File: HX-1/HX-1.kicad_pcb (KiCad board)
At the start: 2 copper layers, 45 x 90 mm, 92 parts, among them J1 USB_C_Receptacle_USB2.0_16P, J10 Conn_01x24, J11 Conn_01x08, J12 USART, J2 Conn_01x02_Socket, J3 I2C, J4 SPI, J6 DEBUG, J8 UART, J9 Conn_01x24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

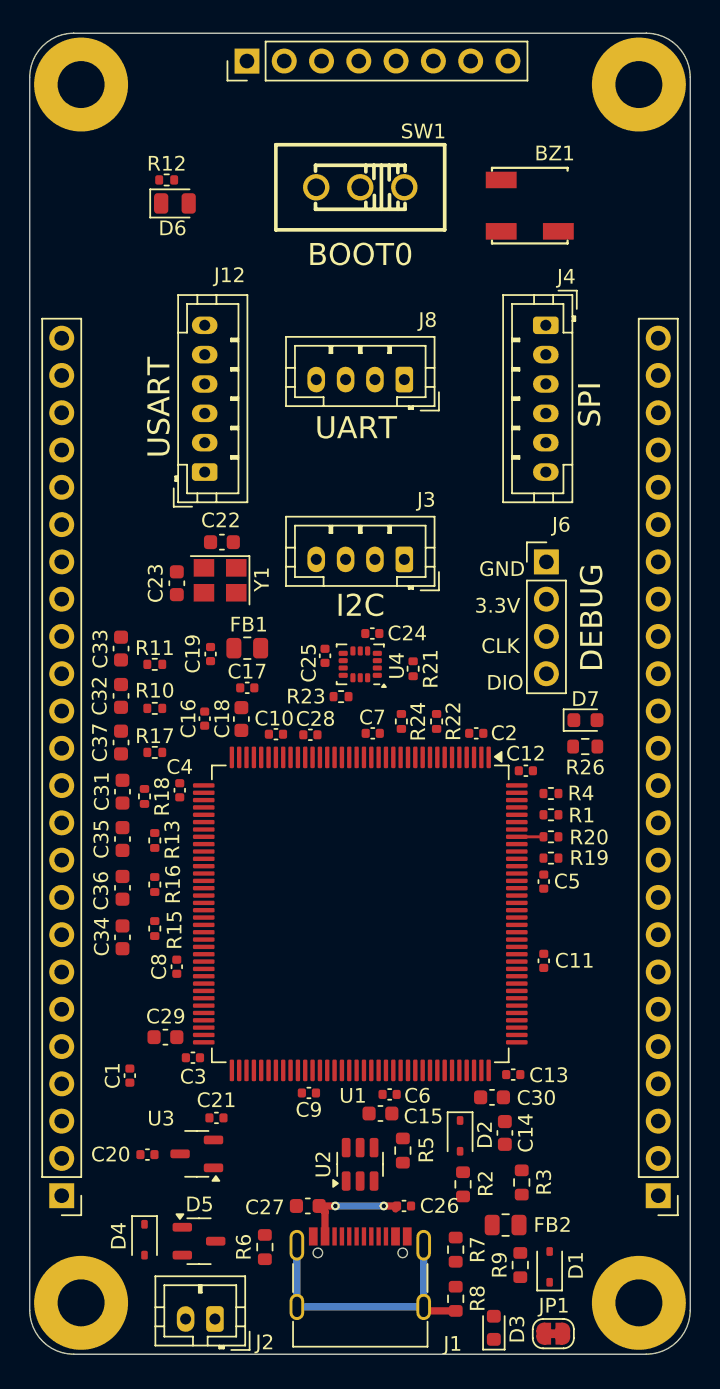
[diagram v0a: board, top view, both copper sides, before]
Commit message: complete initial placement of all components, trace 5V
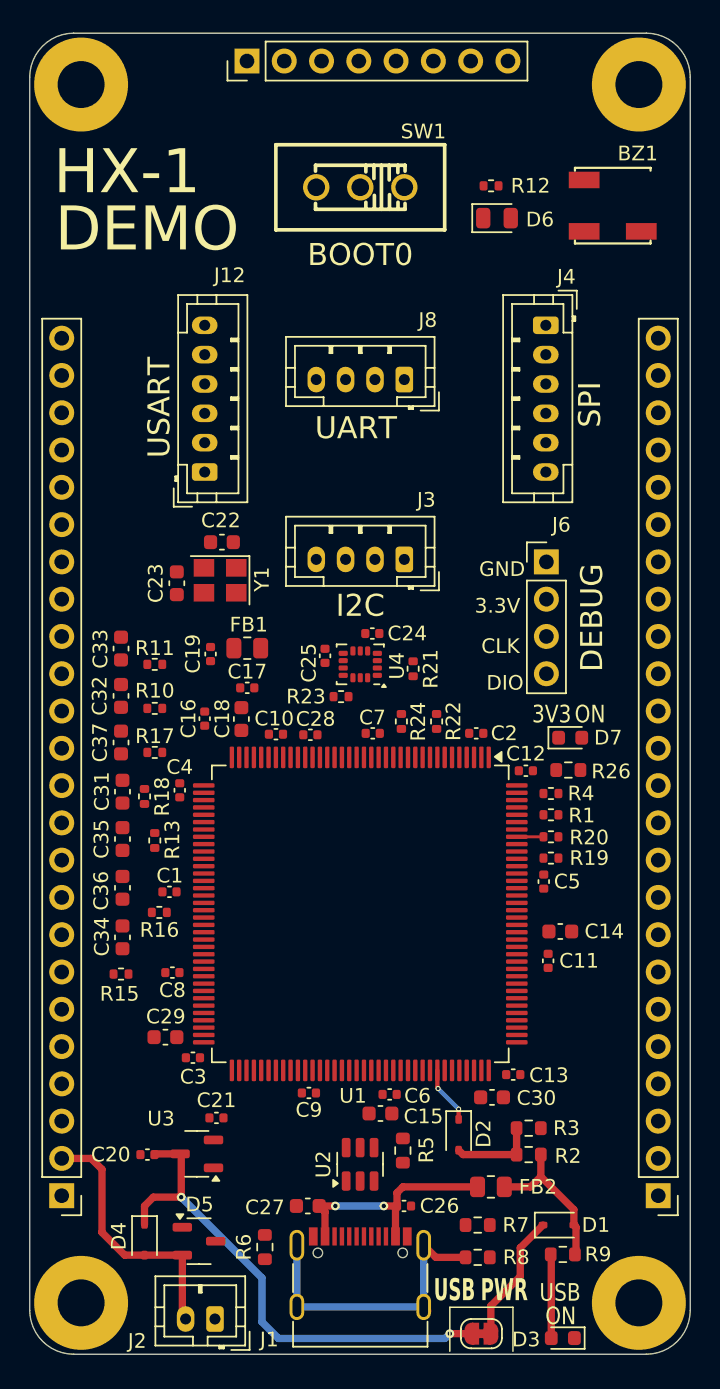
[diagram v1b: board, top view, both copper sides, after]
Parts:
- moved R12 22.1 mm to (153.9, 67.4)
- moved D6 22.0 mm to (154.3, 69.6)
- moved C14 14.2 mm to (158.6, 118.2), turned to 0 degrees
- moved C1 12.8 mm to (132.0, 115.5), turned to 180 degrees
- moved BZ1 5.65 mm to (162.0, 62.8)
- moved R2 4.91 mm to (156.5, 133.4), turned to 180 degrees
- moved JP1 4.90 mm to (153.2, 145.6), turned to 180 degrees
- moved D3 4.75 mm to (158.8, 145.9), turned to 180 degrees
- moved R15 3.86 mm to (128.7, 121.1), turned to 180 degrees
- moved R3 3.73 mm to (156.5, 131.6), turned to 0 degrees
- moved R8 3.20 mm to (153.0, 140.4), turned to 0 degrees
- moved R9 2.99 mm to (158.8, 140.2), turned to 0 degrees
- moved D1 2.91 mm to (158.5, 138.2), turned to 0 degrees
- moved FB2 2.79 mm to (153.9, 135.6)
- moved R7 2.25 mm to (153.0, 138.2), turned to 180 degrees
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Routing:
- net +5V: track 0.00 -> 34.4 mm, vias 0 -> 2
- net V_BATT_RAW: track 0.00 -> 17.9 mm
- net VBUS: track 0.00 -> 10.6 mm
- net /Communication and Debug/VBUS_bridge: track 0.00 -> 8.87 mm
- net vbus_source: track 7.68 -> 16.4 mm
- net /Communication and Debug/vbus_r_divider: track 0.00 -> 5.87 mm
- net /Communication and Debug/USB_LED: track 0.00 -> 5.72 mm
- net USB_VBUS_SENSE: track 0.00 -> 3.94 mm, vias 0 -> 2
- net /Communication and Debug/USB_Shield: track 19.3 -> 20.6 mm
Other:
- board text added: "3V3"
- board text added: "DEMO"
- board text added: "HX-1"
- board text added: "ON"
- board text added: "PWR"
- board text added: "USB"

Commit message: remove 8 pin header on top of board, extend side headers by 4 each to replace pins
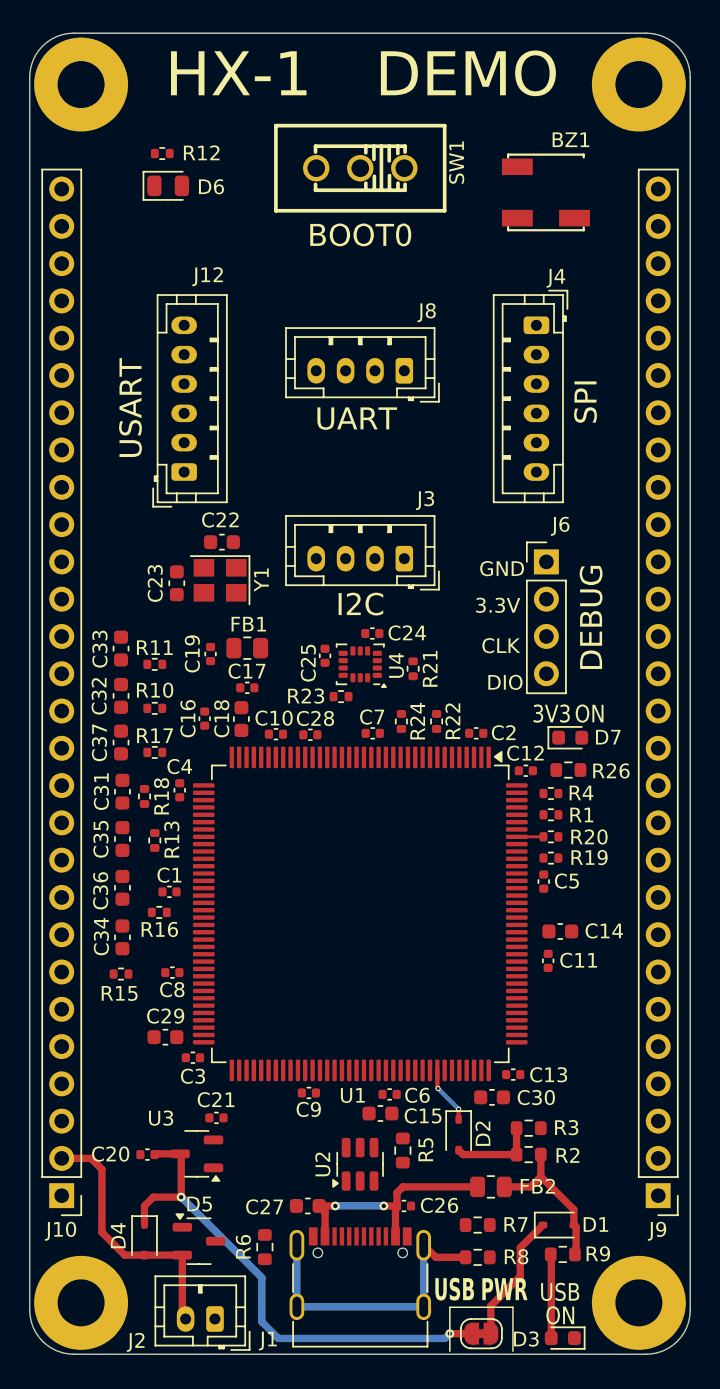
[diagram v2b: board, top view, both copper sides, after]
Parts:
- removed J11: Conn_01x08, Connector_PinHeader_2.54mm:PinHeader_1x08_P2.54mm_Vertical
- J10, J9: footprint Connector_PinHeader_2.54mm:PinHeader_1x24_P2.54mm_Vertical -> Connector_PinHeader_2.54mm:PinHeader_1x28_P2.54mm_Vertical
- moved R12 22.5 mm to (131.5, 65.2)
- moved D6 22.5 mm to (131.9, 67.4)
- moved BZ1 4.64 mm to (157.4, 61.9)
- moved J12 1.40 mm to (133.0, 86.9)
- moved SW1 1.30 mm to (145.0, 66.2)
- moved J4 0.64 mm to (157.0, 76.9)
- moved J8 0.60 mm to (148.0, 80.0)

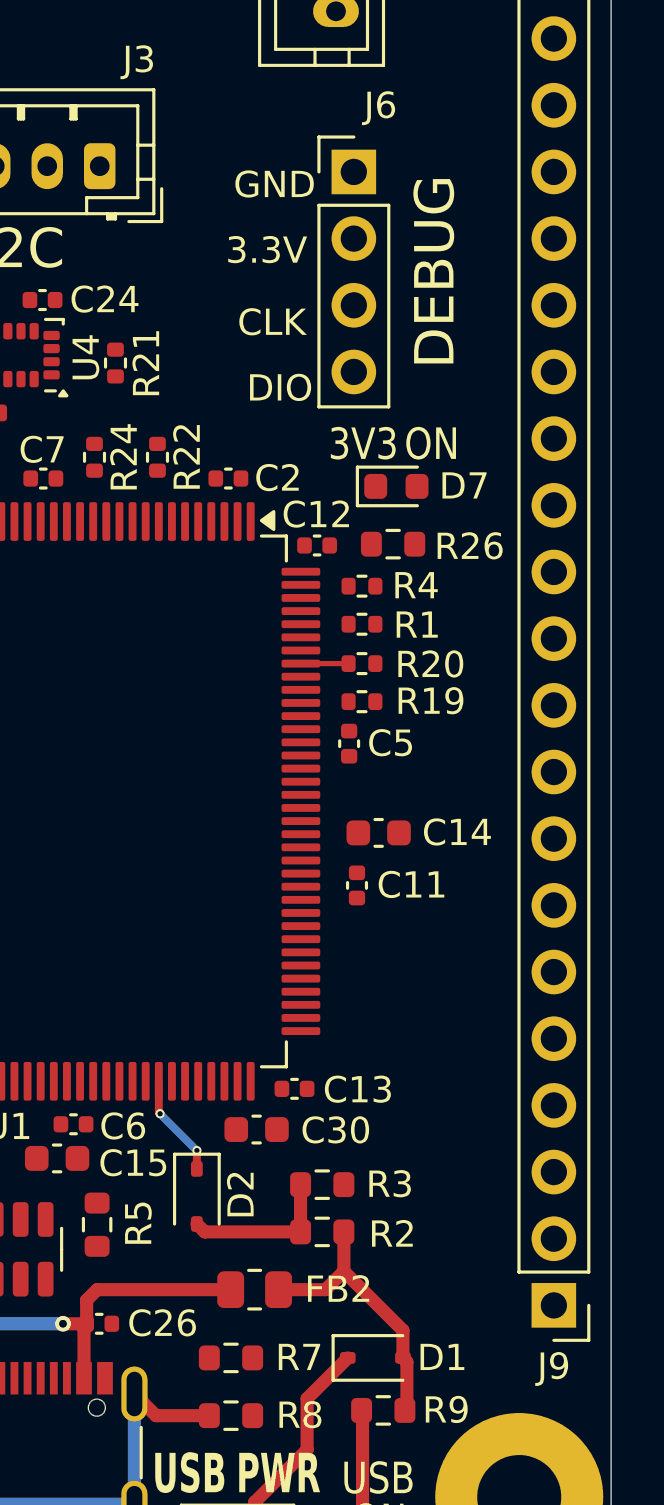
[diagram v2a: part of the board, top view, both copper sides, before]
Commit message: remove GPIO 12 and DEBUG conn, add debug to right header
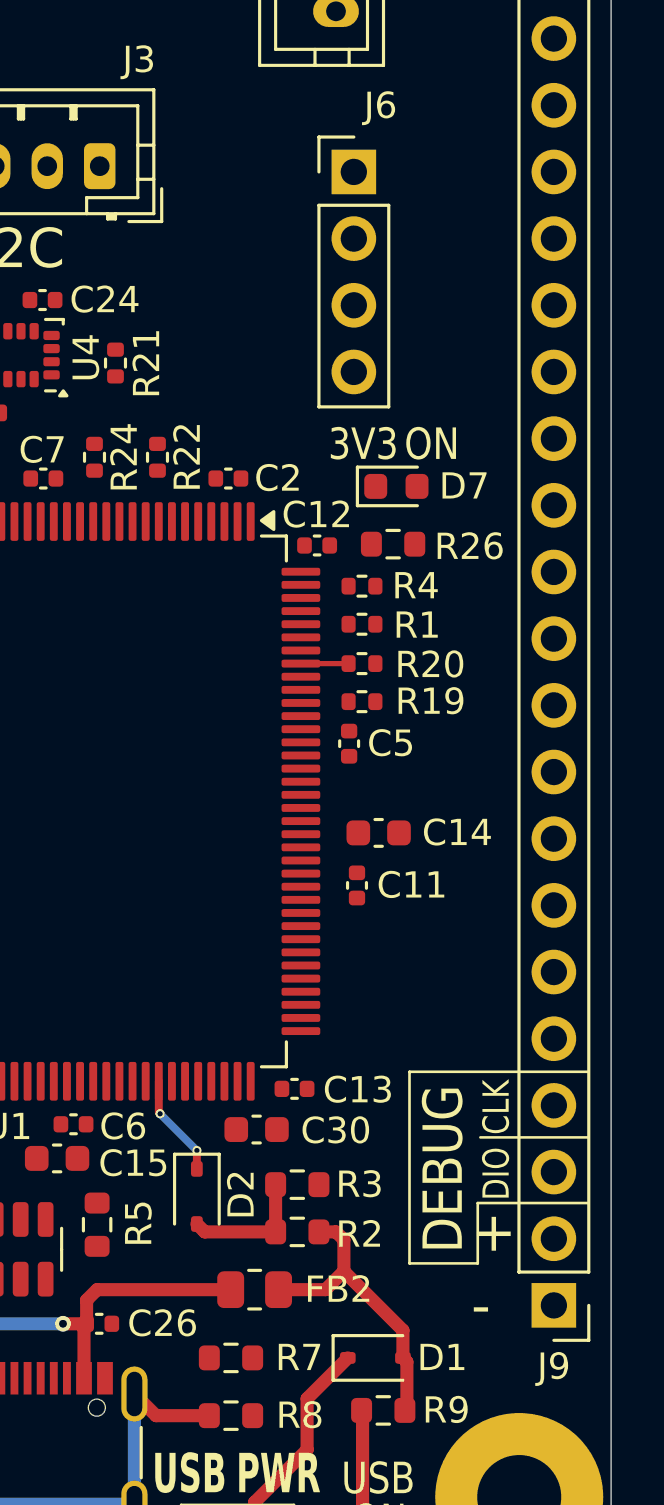
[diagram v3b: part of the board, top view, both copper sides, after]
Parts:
- moved R2 0.95 mm to (155.5, 133.4)
- moved R3 0.95 mm to (155.5, 131.6)
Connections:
- J10 pad 20: /MCU/TIM1_PWM_1- -> /MCU/TIM4_PWM_3
- J10 pad 21: /MCU/TIM1_PWM_1+ -> /MCU/TIM4_PWM_4
- J10 pad 22: /MCU/GPIO_12 -> /MCU/TIM1_PWM_1-
- J10 pad 23: /MCU/GPIO_11 -> /MCU/TIM1_PWM_1+
- J10 pad 24: /MCU/GPIO_10 -> /MCU/GPIO_11
- J10 pad 25: /MCU/GPIO_9 -> /MCU/GPIO_10
- J10 pad 26: /MCU/GPIO_8 -> /MCU/GPIO_9
- J10 pad 27: unconnected-(J10-Pin_27-Pad27) -> /MCU/GPIO_8
- J9 pad 3: /MCU/TIM4_PWM_4 -> /MCU/DEBUG_SWDIO
- J9 pad 4: /MCU/TIM4_PWM_3 -> /MCU/DEBUG_SWCLK
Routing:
- net /Communication and Debug/vbus_r_divider: track 5.87 -> 4.92 mm
- net VBUS: track 10.6 -> 11.3 mm
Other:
- board text added: "+"
- board text added: "-"
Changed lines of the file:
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@@
 	(net 152 "/MCU/DEBUG_SWDIO")
 	(net 153 "/MCU/DEBUG_SWCLK")
-	(net 154 "unconnected-(J10-Pin_27-Pad27)")
 	(footprint "Capacitor_SMD:C_0402_1005Metric"
 		(layer "F.Cu")
@@
 			)
 			(remove_unused_layers no)
-			(net 61 "/MCU/TIM4_PWM_4")
+			(net 152 "/MCU/DEBUG_SWDIO")
 			(pinfunction "Pin_3")
 			(pintype "passive")
@@
 			)
 			(remove_unused_layers no)
-			(net 56 "/MCU/TIM4_PWM_3")
+			(net 153 "/MCU/DEBUG_SWCLK")
 			(pinfunction "Pin_4")
 			(pintype "passive")
@@
 	(footprint "Resistor_SMD:R_0603_1608Metric"
 		(layer "F.Cu")
-		(at 156.475 133.4 180)
+		(at 155.525 133.4 180)
 		(descr "Resistor SMD 0603 (1608 Metric), square (rectangular) end terminal, IPC_7351 nominal, (Body size source: IPC-SM-782 page 72, https://www.pcb-3d.com/wordpress/wp-content/uploads/ipc-sm-782a_amendment_1_and_2.pdf), generated with kicad-footprint-generator")
 		(tags "resistor")
 		(property "Reference" "R2"
-			(at -2.675 -0.1 0)
+			(at -2.375 -0.1 0)
 			(layer "F.SilkS")
 			(effects
@@
 			)
 			(remove_unused_layers no)
-			(net 82 "/MCU/TIM1_PWM_1-")
+			(net 56 "/MCU/TIM4_PWM_3")
 			(pinfunction "Pin_20")
 			(pintype "passive")
@@
 			)
 			(remove_unused_layers no)
-			(net 92 "/MCU/TIM1_PWM_1+")
+			(net 61 "/MCU/TIM4_PWM_4")
 			(pinfunction "Pin_21")
 			(pintype "passive")
@@
 			)
 			(remove_unused_layers no)
-			(net 144 "/MCU/GPIO_12")
+			(net 82 "/MCU/TIM1_PWM_1-")
 			(pinfunction "Pin_22")
 			(pintype "passive")
@@
 			)
 			(remove_unused_layers no)
-			(net 142 "/MCU/GPIO_11")
+			(net 92 "/MCU/TIM1_PWM_1+")
 			(pinfunction "Pin_23")
 			(pintype "passive")
@@
 			)
 			(remove_unused_layers no)
-			(net 146 "/MCU/GPIO_10")
+			(net 142 "/MCU/GPIO_11")
 			(pinfunction "Pin_24")
 			(pintype "passive")
@@
 			)
 			(remove_unused_layers no)
-			(net 138 "/MCU/GPIO_9")
+			(net 146 "/MCU/GPIO_10")
 			(pinfunction "Pin_25")
 			(pintype "passive")
@@
 			)
 			(remove_unused_layers no)
-			(net 48 "/MCU/GPIO_8")
+			(net 138 "/MCU/GPIO_9")
 			(pinfunction "Pin_26")
 			(pintype "passive")
@@
 			)
 			(remove_unused_layers no)
-			(net 154 "unconnected-(J10-Pin_27-Pad27)")
+			(net 48 "/MCU/GPIO_8")
 			(pinfunction "Pin_27")
 			(pintype "passive")
@@
 		)
 		(property "Value" "DEBUG"
-			(at 3.1 3.8 90)
+			(at 3.42 37.98 90)
 			(layer "F.SilkS")
 			(effects
 				(font
-					(size 1.5 1.5)
+					(size 1.5 1.3)
 					(thickness 0.2)
 				)
@@
 	(footprint "Resistor_SMD:R_0603_1608Metric"
 		(layer "F.Cu")
-		(at 156.475 131.6)
+		(at 155.525 131.6)
 		(descr "Resistor SMD 0603 (1608 Metric), square (rectangular) end terminal, IPC_7351 nominal, (Body size source: IPC-SM-782 page 72, https://www.pcb-3d.com/wordpress/wp-content/uploads/ipc-sm-782a_amendment_1_and_2.pdf), generated with kicad-footprint-generator")
 		(tags "resistor")
 		(property "Reference" "R3"
-			(at 2.575 0 0)
+			(at 2.375 0 0)
 			(layer "F.SilkS")
 			(effects
@@
 	)
 	(gr_line
+		(start 162.4 134.6)
+		(end 162.4 132.3)
+		(stroke
+			(width 0.1)
+			(type default)
+		)
+		(layer "F.SilkS")
+	)
+	(gr_line
 		(start 155.4 146.8)
 		(end 155.4 143.8)
@@
 	)
 	(gr_line
+		(start 159.8 134.6)
+		(end 162.4 134.6)
+		(stroke
+			(width 0.1)
+			(type default)
+		)
+		(layer "F.SilkS")
+	)
+	(gr_line
 		(start 151.1 143.8)
 		(end 155.4 143.8)
@@
 	)
 	(gr_line
+		(start 162.5 129.8)
+		(end 166.6 129.8)
+		(stroke
+			(width 0.1)
+			(type default)
+		)
+		(layer "F.SilkS")
+	)
+	(gr_line
+		(start 159.8 127.3)
+		(end 166.6 127.3)
+		(stroke
+			(width 0.1)
+			(type default)
+		)
+		(layer "F.SilkS")
+	)
+	(gr_line
+		(start 159.8 127.3)
+		(end 159.8 134.6)
+		(stroke
+			(width 0.1)
+			(type default)
+		)
+		(layer "F.SilkS")
+	)
+	(gr_line
+		(start 166.6 132.3)
+		(end 162.4 132.3)
+		(stroke
+			(width 0.1)
+			(type default)
+		)
+		(layer "F.SilkS")
+	)
+	(gr_line
 		(start 151.1 146.8)
 		(end 151.1 143.8)
@@
 		)
 	)
-	(gr_text "GND"
-		(at 153.09 94.1 0)
-		(layer "F.SilkS")
-		(effects
-			(font
-				(size 1 1)
-				(thickness 0.15)
-			)
-			(justify left bottom)
-		)
-	)
 	(gr_text "DIO"
-		(at 153.59 101.85 0)
+		(at 163.7 132.2 90)
 		(layer "F.SilkS")
 		(effects
 			(font
-				(size 1 1)
+				(size 1 0.8)
 				(thickness 0.15)
 			)
@@
 		)
 	)
+	(gr_text "+"
+		(at 162.15 134.3 0)
+		(layer "F.SilkS")
+		(effects
+			(font
+				(size 1.5 1.5)
+				(thickness 0.2)
+			)
+			(justify left bottom)
+		)
+	)
 	(gr_text "CLK"
-		(at 153.24 99.35 0)
+		(at 163.7 129.7 90)
 		(layer "F.SilkS")
 		(effects
 			(font
-				(size 1 1)
+				(size 1 0.8)
 				(thickness 0.15)
 			)
@@
 		)
 	)
+	(gr_text "-"
+		(at 162.15 137.1 0)
+		(layer "F.SilkS")
+		(effects
+			(font
+				(size 1.5 1.5)
+				(thickness 0.2)
+			)
+			(justify left bottom)
+		)
+	)
 	(gr_text "ON"
 		(at 159.6 104.1 0)
@@
 		)
 	)
-	(gr_text "3.3V"
-		(at 152.79 96.6 0)
-		(layer "F.SilkS")
-		(effects
-			(font
-				(size 1 1)
-				(thickness 0.15)
-			)
-			(justify left bottom)
-		)
-	)
 	(gr_text "3V3"
 		(at 156.7 104.1 0)
@@
 	)
 	(segment
-		(start 155.65 133.4)
-		(end 155.65 131.6)
+		(start 154.7 133.4)
+		(end 154.7 131.6)
 		(width 0.5)
 		(layer "F.Cu")
@@
 	)
 	(segment
-		(start 155.65 133.4)
-		(end 152 133.4)
+		(start 152 133.4)
+		(end 154.7 133.4)
 		(width 0.5)
 		(layer "F.Cu")
@@
 	)
 	(segment
+		(start 157.3 133.7)
+		(end 157 133.4)
+		(width 0.5)
+		(layer "F.Cu")
+		(net 34)
+	)
+	(segment
 		(start 159.7 138.35)
 		(end 159.55 138.2)
@@
 	)
 	(segment
-		(start 159.7 140.2)
-		(end 159.7 138.35)
+		(start 157 133.4)
+		(end 156.35 133.4)
 		(width 0.5)
 		(layer "F.Cu")
@@
 	)
 	(segment
-		(start 157.3 134.9)
-		(end 157.3 133.4)
+		(start 159.7 140.2)
+		(end 159.7 138.35)
 		(width 0.5)
 		(layer "F.Cu")
@@
 		(width 0.5)
 		(layer "F.Cu")
+		(net 34)
+	)
+	(segment
+		(start 157.3 134.9)
+		(end 157.3 133.7)
+		(width 0.5)
+		(layer "F.Cu")
